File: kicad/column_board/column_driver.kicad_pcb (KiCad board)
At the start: 2 copper layers, 100 x 100 mm, 104 parts, among them J1 Panel column connector (femal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, J2 PWR_CHAIN_IN, J3 PWR_CHAIN_OUT, J4 DATA_CHAIN_IN, J5 DATA_CHAIN_OUT, U1 TPIC6B595, U10 TPIC6B595, U11 TPIC6B595, U12 TBD62783, U2 TPIC6B595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

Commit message: Nearly done routing column board.
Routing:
- net RC_DATA_OUT: track 0.00 -> 88.7 mm, vias 0 -> 3
- net +24V: track 246.9 -> 324.0 mm
- net RC_DATA: track 0.00 -> 49.4 mm, vias 0 -> 2
- net ~COL_EN: track 206.2 -> 245.6 mm
- net COL4: track 79.1 -> 43.3 mm, vias 4 -> 2
- net Net-(U5-Pad18): track 0.00 -> 34.4 mm, vias 0 -> 2
- net Net-(U10-Pad3): track 0.00 -> 33.4 mm, vias 0 -> 2
- net GND: track 54.0 -> 85.6 mm, vias 36 -> 37
- net RC_SHIFT_CLK: track 196.5 -> 227.8 mm
- net ~RC_CLEAR: track 216.0 -> 246.0 mm
- net Net-(D127-Pad2): track 25.5 -> 54.6 mm
- net COL_REG_CLK: track 186.7 -> 213.7 mm
- net Net-(U7-Pad18): track 0.00 -> 17.7 mm
- net Net-(U4-Pad18): track 0.00 -> 17.0 mm
- net Net-(U10-Pad18): track 0.00 -> 16.2 mm
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
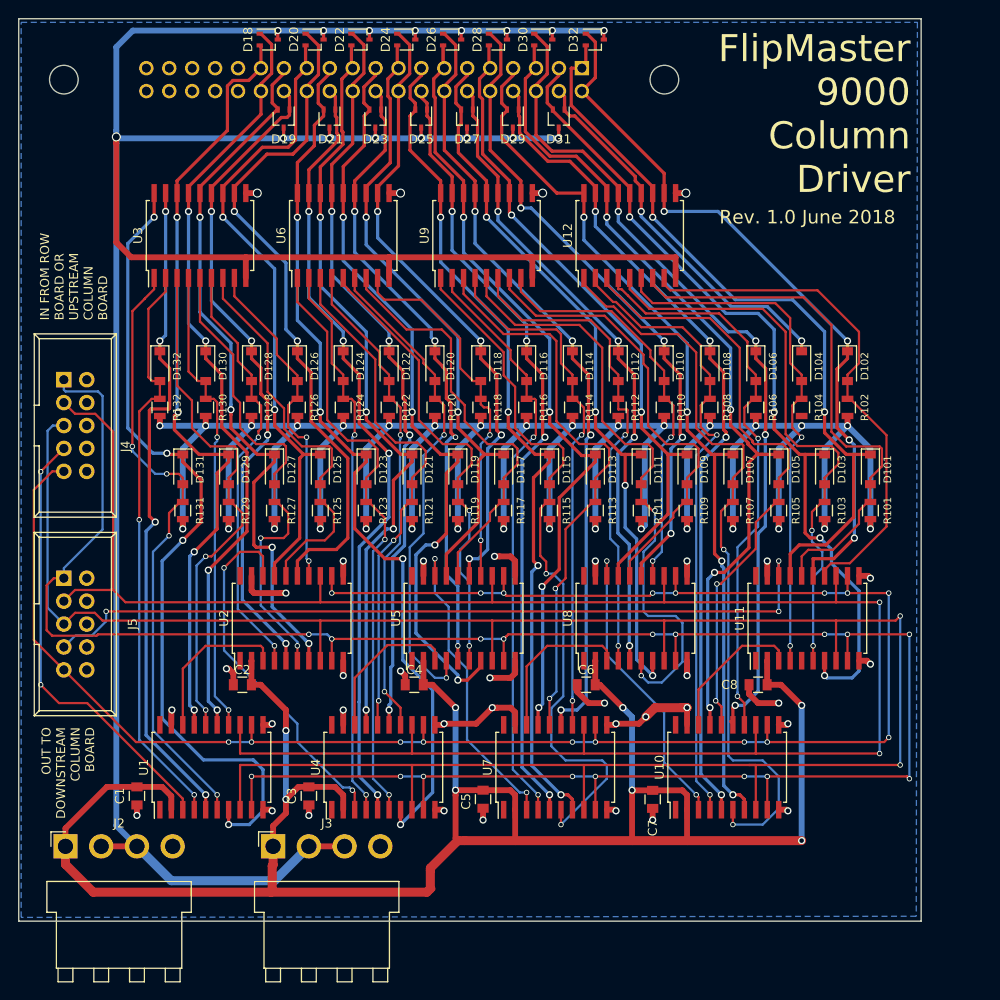
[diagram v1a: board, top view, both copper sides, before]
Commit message: All connections routed. Board still ugly.
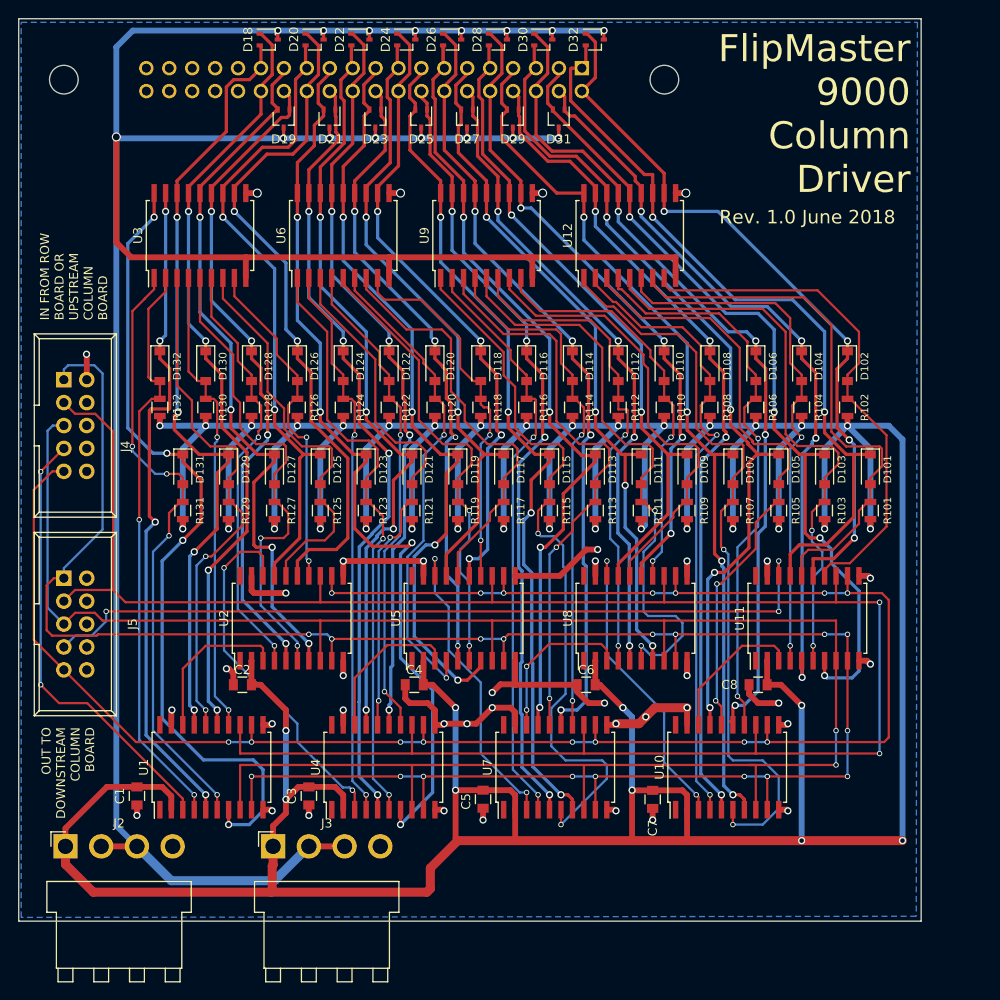
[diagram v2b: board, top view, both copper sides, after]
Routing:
- net +5V: track 543.0 -> 606.2 mm, vias 40 -> 41
- net COL4: track 43.3 -> 82.6 mm, vias 2 -> 4
- net GND: track 85.6 -> 116.0 mm, vias 37 -> 38
- net ~RC_CLEAR: track 246.0 -> 226.6 mm
- net ~COL_EN: track 245.6 -> 231.4 mm
- net COL11: track 80.8 -> 77.5 mm
- net COL23: track 98.2 -> 101.2 mm
- net Net-(D111-Pad2): track 68.9 -> 66.1 mm
- net Net-(D115-Pad2): track 80.7 -> 81.5 mm
- net COL_REG_CLK: track 213.7 -> 213.0 mm, vias 17 -> 15
- net COL1: track 83.8 -> 84.4 mm
- net Net-(D120-Pad2): track 55.2 -> 54.7 mm
- net Net-(U7-Pad18): track 17.7 -> 17.9 mm, vias 0 -> 2

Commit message: Parts positioned
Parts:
- moved D132 45.9 mm to (44.5, 109.2), turned to 180 degrees
- moved D124 45.8 mm to (63.5, 109.2), turned to 180 degrees
- moved D116 45.7 mm to (82.5, 109.2), turned to 180 degrees
- moved D108 45.7 mm to (101.6, 109.2), turned to 180 degrees
- moved R132 43.8 mm to (43.8, 111.8), turned to 180 degrees
- moved R124 43.7 mm to (62.9, 111.8), turned to 180 degrees
- moved R108 43.7 mm to (101.0, 111.8), turned to 180 degrees
- moved R116 43.7 mm to (81.9, 111.8), turned to 180 degrees
- moved D131 34.9 mm to (49.5, 109.2), turned to 180 degrees
- moved D123 34.7 mm to (68.6, 109.2), turned to 180 degrees
- moved D115 34.5 mm to (87.6, 109.2), turned to 180 degrees
- moved D107 34.4 mm to (106.7, 109.2), turned to 180 degrees
- moved R131 32.8 mm to (48.9, 111.8), turned to 180 degrees
- moved R123 32.6 mm to (67.9, 111.8), turned to 180 degrees
- moved R115 32.4 mm to (87.0, 111.8), turned to 180 degrees
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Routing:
- net +24V: track 323.9 -> 130.1 mm
- net +5V: track 606.2 -> 435.6 mm, vias 41 -> 23
- net ~COL_EN: track 231.4 -> 67.5 mm, vias 17 -> 4
- net RC_SHIFT_CLK: track 227.8 -> 67.5 mm, vias 2 -> 4
- net ~RC_CLEAR: track 226.6 -> 95.8 mm, vias 2 -> 5
- net COL_REG_CLK: track 213.0 -> 97.1 mm, vias 15 -> 4
- net RC_DATA_OUT: track 88.7 -> 0.00 mm, vias 3 -> 0
- net COL31: track 90.6 -> 4.34 mm, vias 4 -> 0
- net GND: track 116.0 -> 30.0 mm, vias 38 -> 24
- net COL23: track 101.2 -> 20.3 mm, vias 4 -> 0
- net Net-(D107-Pad2): track 84.2 -> 5.59 mm, vias 2 -> 0
- net Net-(D115-Pad2): track 81.5 -> 5.59 mm, vias 2 -> 0
- net COL3: track 92.7 -> 18.1 mm, vias 4 -> 0
- net COL7: track 98.8 -> 24.8 mm, vias 4 -> 0
- net COL15: track 94.4 -> 20.6 mm, vias 4 -> 0
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
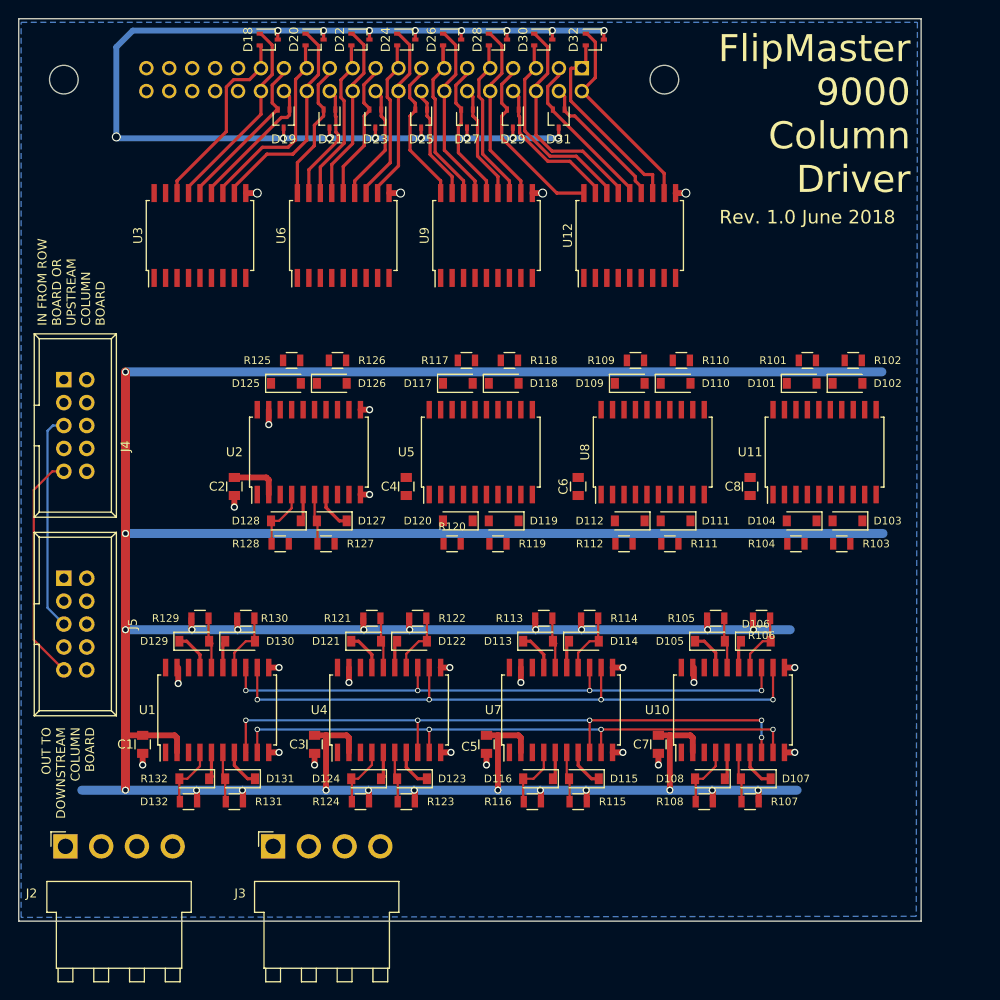
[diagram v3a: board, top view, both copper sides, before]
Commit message: About to move high side drivers
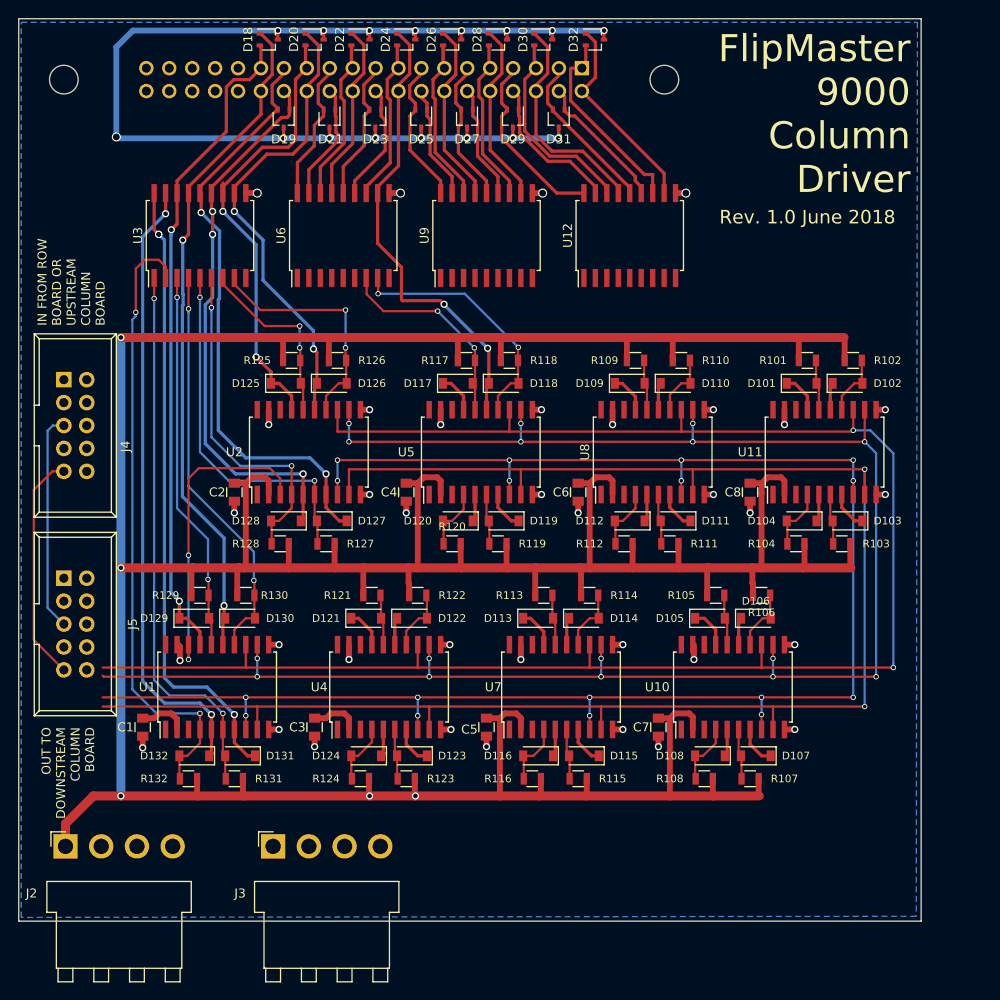
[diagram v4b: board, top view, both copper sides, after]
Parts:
- moved D105 2.54 mm to (101.6, 91.4)
- moved D106 2.54 mm to (106.7, 91.4)
- moved D113 2.54 mm to (82.5, 91.4)
- moved D114 2.54 mm to (87.6, 91.4)
- moved D121 2.54 mm to (63.5, 91.4)
- moved D122 2.54 mm to (68.6, 91.4)
- moved D129 2.54 mm to (44.5, 91.4)
- moved D130 2.54 mm to (49.5, 91.4)
- moved R107 2.54 mm to (106.0, 109.2)
- moved R108 2.54 mm to (101.0, 109.2)
- moved R115 2.54 mm to (87.0, 109.2)
- moved R116 2.54 mm to (81.9, 109.2)
- moved R123 2.54 mm to (67.9, 109.2)
- moved R124 2.54 mm to (62.9, 109.2)
- moved R131 2.54 mm to (48.9, 109.2)
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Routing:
- net RC_SHIFT_CLK: track 67.5 -> 194.1 mm, vias 4 -> 2
- net COL_REG_CLK: track 97.1 -> 223.7 mm, vias 4 -> 16
- net ~RC_CLEAR: track 95.8 -> 218.0 mm, vias 5 -> 17
- net ~COL_EN: track 67.5 -> 189.4 mm, vias 4 -> 2
- net COL32: track 3.39 -> 69.3 mm, vias 0 -> 2
- net COL31: track 4.34 -> 69.6 mm, vias 0 -> 3
- net Net-(D132-Pad2): track 7.10 -> 69.5 mm, vias 0 -> 2
- net Net-(D131-Pad2): track 5.59 -> 62.2 mm, vias 0 -> 2
- net COL30: track 25.7 -> 75.1 mm, vias 0 -> 2
- net COL29: track 25.8 -> 73.6 mm, vias 0 -> 2
- net COL27: track 22.6 -> 66.1 mm, vias 0 -> 2
- net COL28: track 18.5 -> 61.2 mm, vias 0 -> 3
- net +5V: track 435.6 -> 474.8 mm, vias 23 -> 5
- net Net-(D130-Pad2): track 7.03 -> 45.4 mm, vias 0 -> 2
- net Net-(D129-Pad2): track 5.95 -> 42.6 mm, vias 0 -> 2
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
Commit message: Final routing
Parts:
- moved J5 22.1 mm to (30.0, 64.9)
- moved J4 22.0 mm to (30.0, 87.0)
- moved U12 15.2 mm to (108.0, 48.9)
- moved U9 10.2 mm to (87.0, 48.9)
- moved U6 5.08 mm to (66.0, 48.9)
- moved U3 0.13 mm to (45.1, 48.9)
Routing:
- net +24V: track 130.1 -> 264.5 mm, vias 16 -> 17
- net COL7: track 24.8 -> 109.4 mm, vias 0 -> 2
- net COL8: track 19.5 -> 96.2 mm, vias 0 -> 2
- net COL15: track 20.6 -> 94.1 mm, vias 0 -> 2
- net COL16: track 15.9 -> 86.6 mm, vias 0 -> 2
- net COL5: track 26.9 -> 91.6 mm, vias 0 -> 3
- net COL24: track 16.4 -> 80.9 mm, vias 0 -> 2
- net COL23: track 20.3 -> 84.0 mm, vias 0 -> 2
- net COL6: track 28.4 -> 89.9 mm, vias 0 -> 3
- net COL14: track 23.6 -> 85.1 mm, vias 0 -> 2
- net COL13: track 22.7 -> 83.5 mm, vias 0 -> 2
- net COL3: track 22.5 -> 80.1 mm, vias 0 -> 2
- net Net-(D123-Pad2): track 6.05 -> 62.8 mm, vias 0 -> 2
- net COL11: track 20.4 -> 75.6 mm, vias 0 -> 2
- net COL21: track 22.5 -> 75.8 mm, vias 0 -> 2
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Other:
- board text added: "Rev. 1.0b June 2018"
- board text removed: "Rev. 1.0 June 2018"

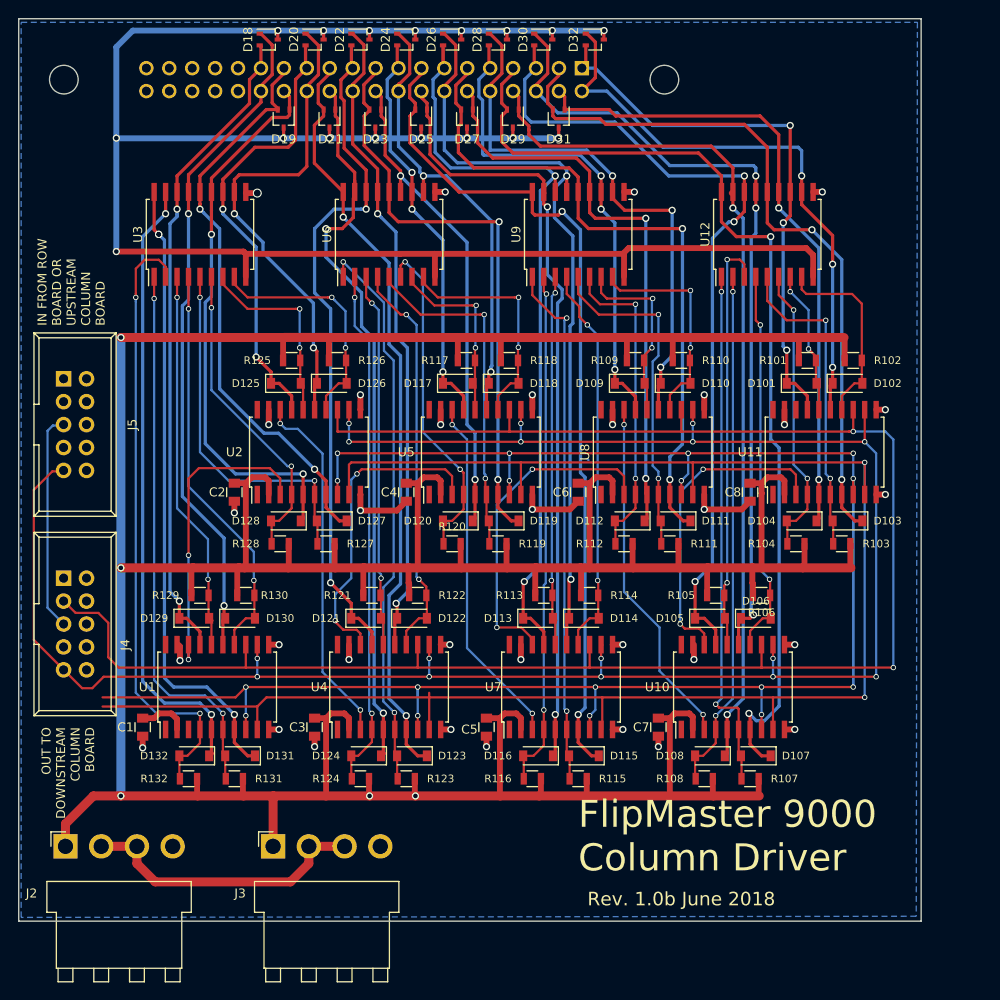
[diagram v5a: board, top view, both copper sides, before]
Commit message: Fully routed column board
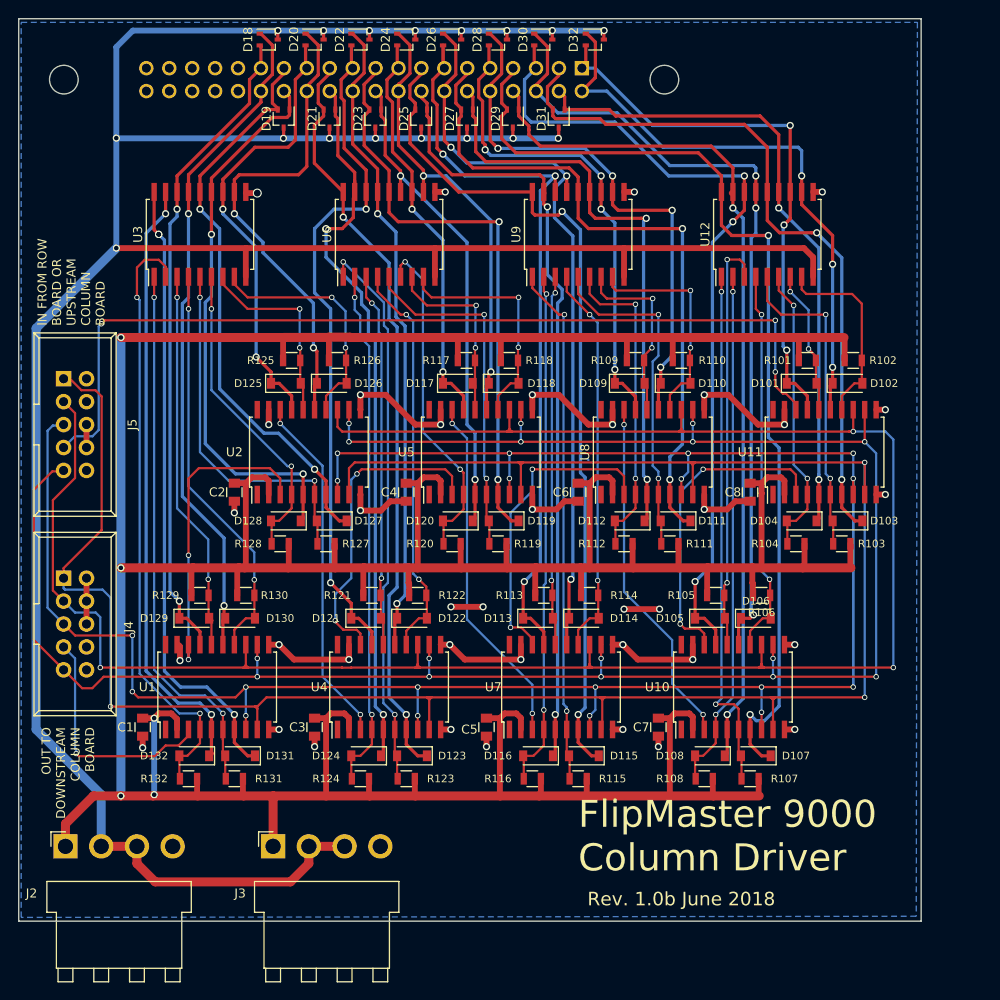
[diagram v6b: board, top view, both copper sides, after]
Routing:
- net RC_DATA_OUT: track 0.00 -> 102.5 mm, vias 0 -> 3
- net +24V: track 264.5 -> 339.3 mm
- net GND: track 60.9 -> 124.7 mm
- net ~COL_EN: track 196.0 -> 244.2 mm, vias 2 -> 3
- net RC_SHIFT_CLK: track 204.7 -> 234.3 mm, vias 2 -> 3
- net RC_DATA: track 0.00 -> 26.6 mm, vias 0 -> 1
- net ~RC_CLEAR: track 250.0 -> 260.5 mm, vias 17 -> 19
- net +5V: track 489.0 -> 497.7 mm
- net (no net): track 0.18 -> 7.67 mm, vias 0 -> 4
- net Net-(U7-Pad18): track 36.8 -> 34.6 mm
- net Net-(D132-Pad2): track 69.2 -> 67.6 mm
- net COL32: track 69.3 -> 68.1 mm
- net COL12: track 64.7 -> 65.7 mm
- net Net-(U2-Pad18): track 39.9 -> 39.1 mm
- net COL14: track 85.1 -> 84.3 mm, vias 2 -> 3
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
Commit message: Cleanup on column board
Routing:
- net RC_SHIFT_CLK: track 234.3 -> 232.8 mm
- net GND: track 124.7 -> 125.8 mm
